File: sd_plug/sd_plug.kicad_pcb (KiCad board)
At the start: 2 copper layers, 44.2 x 20 mm, 4 parts, among them J1 MUX CONNECT TOP, J2 MUX CONNECT BOTTOM, P1 uSD PADS

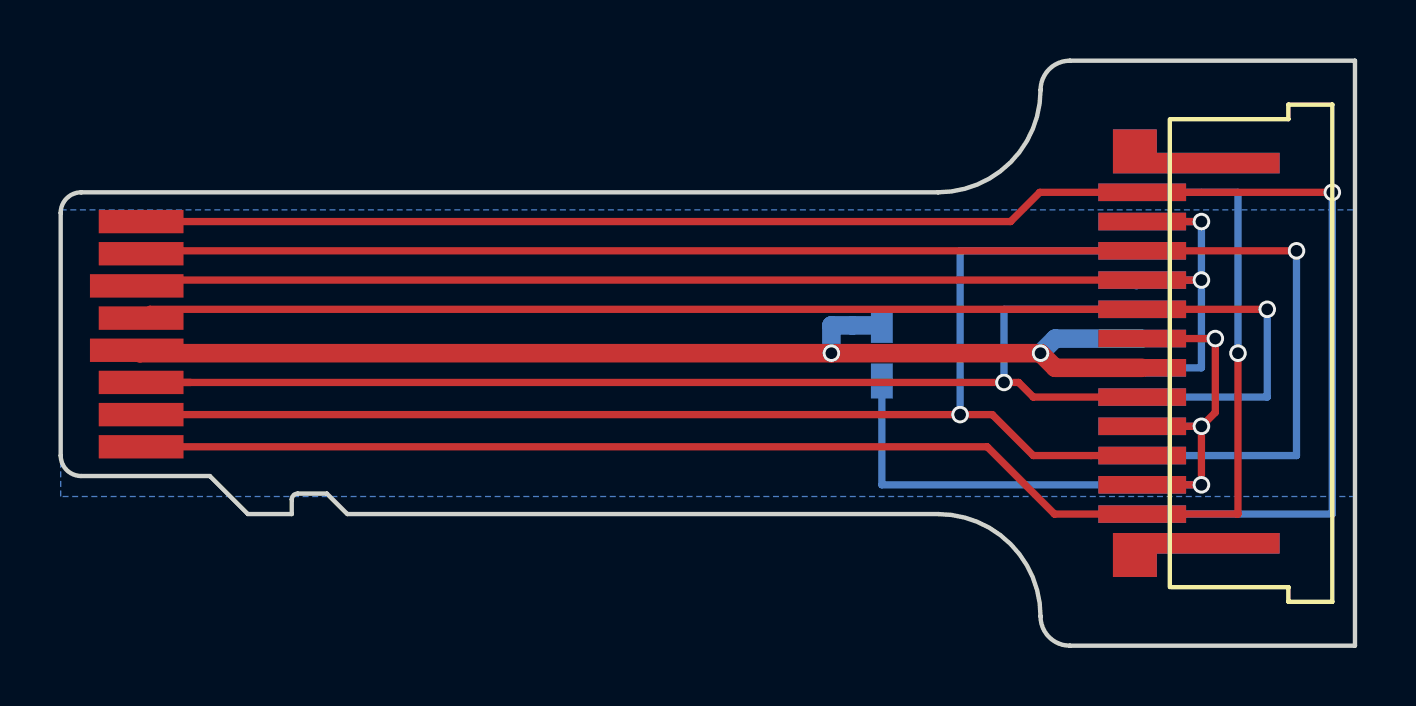
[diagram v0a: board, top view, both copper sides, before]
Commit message: renumbered FFC on adapter board
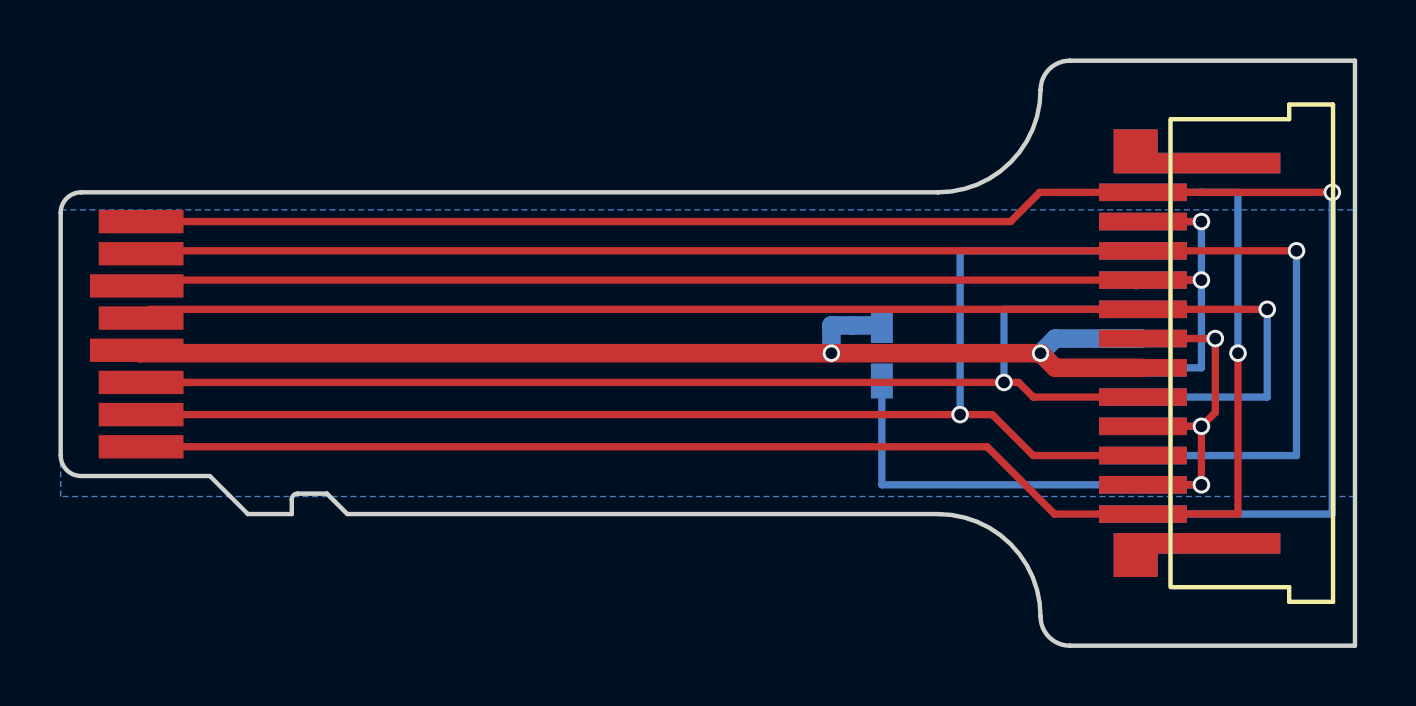
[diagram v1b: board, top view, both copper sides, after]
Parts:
- J1, J2: footprint sd_mux_footprints:FFC_connector_SFW12R-2STE1LF -> sd_plug_footprints:FFC_connector_SFW12R-2STE1LF_reversed
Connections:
- J1 pad 1: DAT2 -> DAT1
- J1 pad 10: DAT0 -> DAT3/CD
- J1 pad 12: DAT1 -> DAT2
- J1 pad 3: DAT3/CD -> DAT0
- J1 pad 5: CMD -> CLK
- J1 pad 6: VDD -> VSS
- J1 pad 7: VSS -> VDD
- J1 pad 8: CLK -> CMD
- J2 pad 1: DAT2 -> DAT1
- J2 pad 10: DAT0 -> DAT3/CD
- J2 pad 12: DAT1 -> DAT2
- J2 pad 3: DAT3/CD -> DAT0
- J2 pad 5: CMD -> CLK
- J2 pad 6: VDD -> VSS
- J2 pad 7: VSS -> VDD
- J2 pad 8: CLK -> CMD

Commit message: redid mounting holes on mux board
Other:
- rule pad_to_mask_clearance: 0.05 -> 0.127
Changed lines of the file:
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@@
   (general
     (links 26)
-    (no_connects 24)
+    (no_connects 0)
     (area 128.674999 97.574999 173.075001 117.725001)
     (thickness 1.6)
@@
     (pad_size 1.524 1.524)
     (pad_drill 0.762)
-    (pad_to_mask_clearance 0.05)
+    (pad_to_mask_clearance 0.127)
+    (solder_mask_min_width 0.0254)
     (aux_axis_origin 0 0)
     (grid_origin 128.75 102.15)
     (visible_elements FFFFFF7F)
     (pcbplotparams
-      (layerselection 0x00030_80000001)
+      (layerselection 0x010f0_80000001)
       (usegerberextensions false)
       (excludeedgelayer true)
@@
       (padsonsilk false)
       (subtractmaskfromsilk false)
-      (outputformat 1)
+      (outputformat 4)
       (mirror false)
-      (drillshape 1)
+      (drillshape 0)
       (scaleselection 1)
-      (outputdirectory ""))
+      (outputdirectory ../../pdfs/sd_plug/))
   )
   (net 0 "")

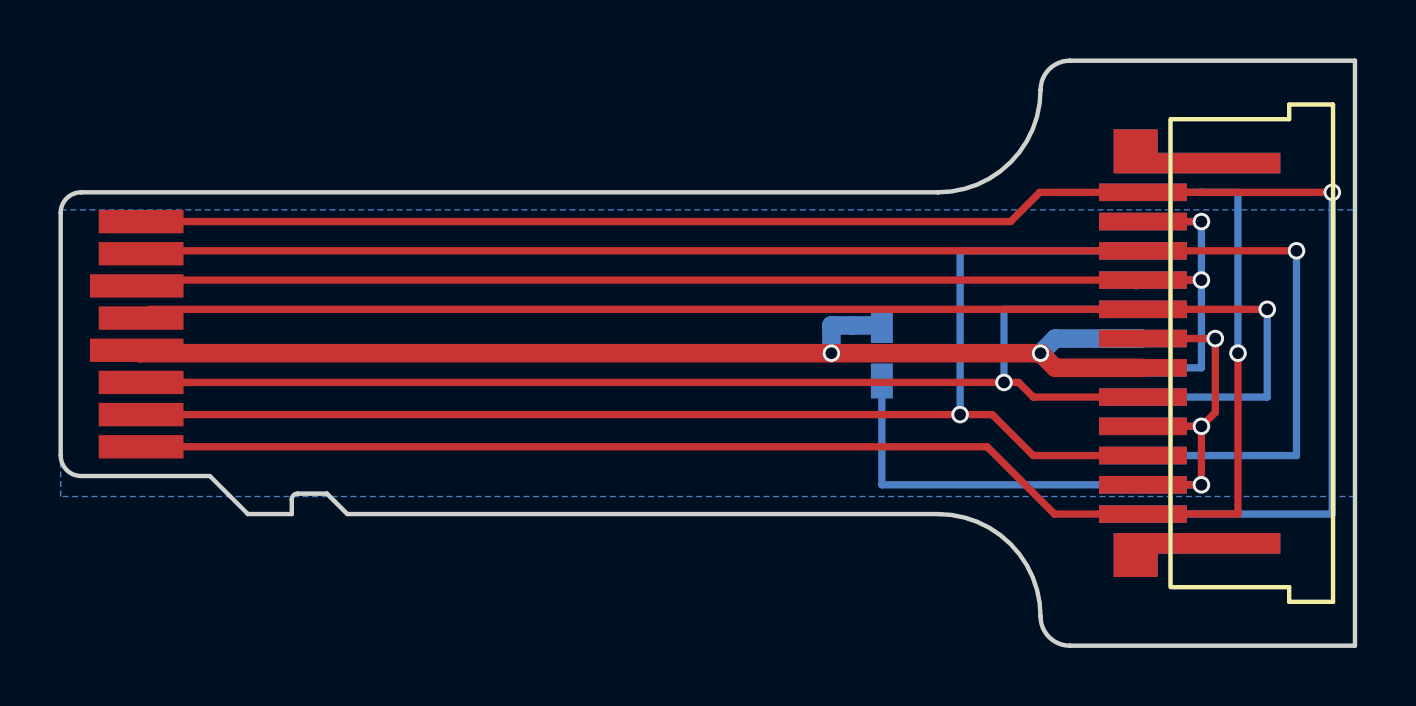
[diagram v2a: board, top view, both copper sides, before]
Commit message: rerouted mux board to fix FFC flip issue and fix tracks that had become unalaigned from the grid
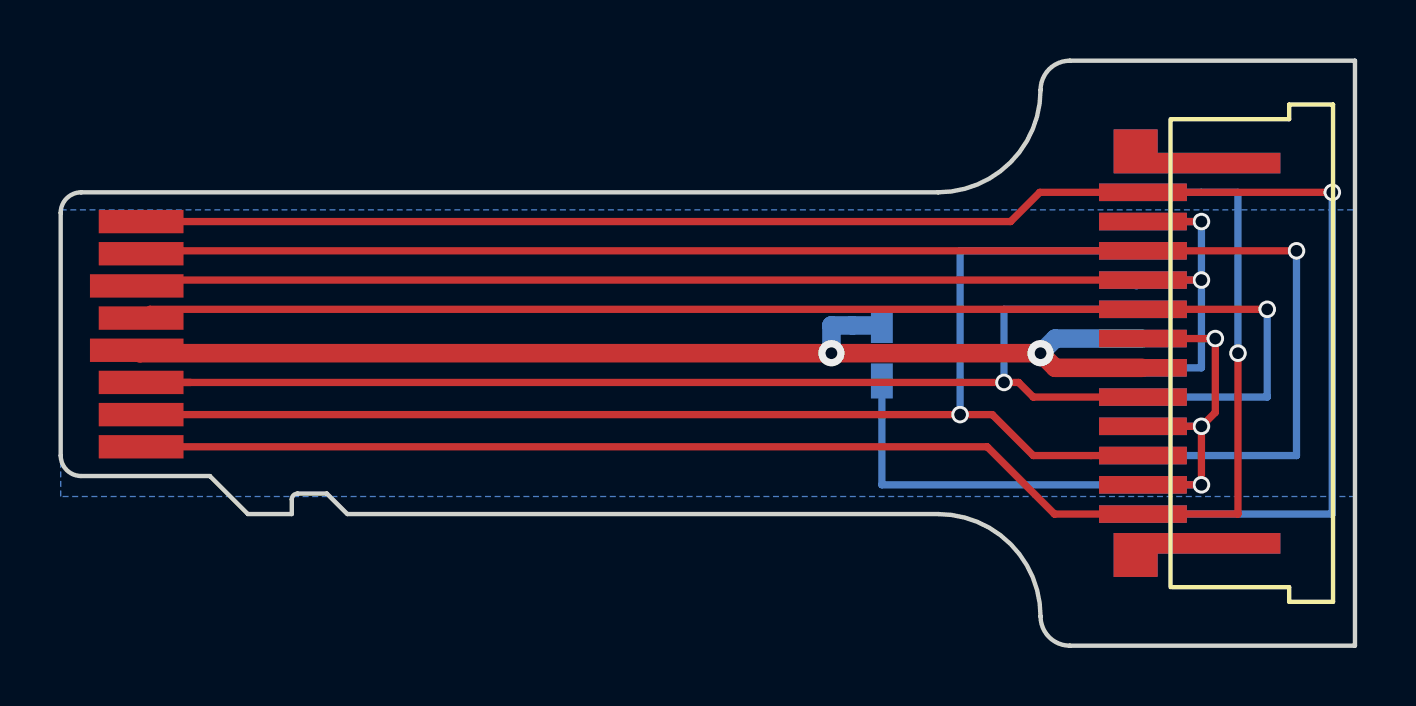
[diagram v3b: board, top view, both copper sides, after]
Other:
- rule pad_to_mask_clearance: 0.127 -> 0.15
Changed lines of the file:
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@@
     (links 26)
     (no_connects 0)
-    (area 128.674999 97.574999 173.075001 117.725001)
+    (area 112.350001 97.574999 173.075002 117.725001)
     (thickness 1.6)
     (drawings 26)
@@
     (pad_size 1.524 1.524)
     (pad_drill 0.762)
-    (pad_to_mask_clearance 0.127)
+    (pad_to_mask_clearance 0.15)
     (solder_mask_min_width 0.0254)
     (aux_axis_origin 0 0)
@@
   (segment (start 156.825 106.7) (end 155.815 106.7) (width 0.635) (layer B.Cu) (net 1))
   (segment (start 131.439972 107.639972) (end 131.35 107.55) (width 0.25) (layer F.Cu) (net 1))
-  (via (at 162.25 107.65) (size 0.6) (drill 0.4) (layers F.Cu B.Cu) (net 1))
+  (via (at 162.25 107.65) (size 0.9) (drill 0.4) (layers F.Cu B.Cu) (net 1))
   (segment (start 165.725 107.15) (end 162.75 107.15) (width 0.635) (layer B.Cu) (net 1))
   (segment (start 162.75 107.15) (end 162.25 107.65) (width 0.635) (layer B.Cu) (net 1))
@@
   (segment (start 162.25 107.65) (end 155.1 107.65) (width 0.635) (layer F.Cu) (net 1))
   (segment (start 162.75 108.15) (end 162.25 107.65) (width 0.635) (layer F.Cu) (net 1))
-  (via (at 155.1 107.65) (size 0.6) (drill 0.4) (layers F.Cu B.Cu) (net 1))
+  (via (at 155.1 107.65) (size 0.9) (drill 0.4) (layers F.Cu B.Cu) (net 1) (status 1000000))
   (segment (start 155.1 106.7) (end 155.1 107.65) (width 0.635) (layer B.Cu) (net 1))
   (segment (start 155.815 106.7) (end 155.1 106.7) (width 0.635) (layer B.Cu) (net 1))

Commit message: minor routing change to sd plug board
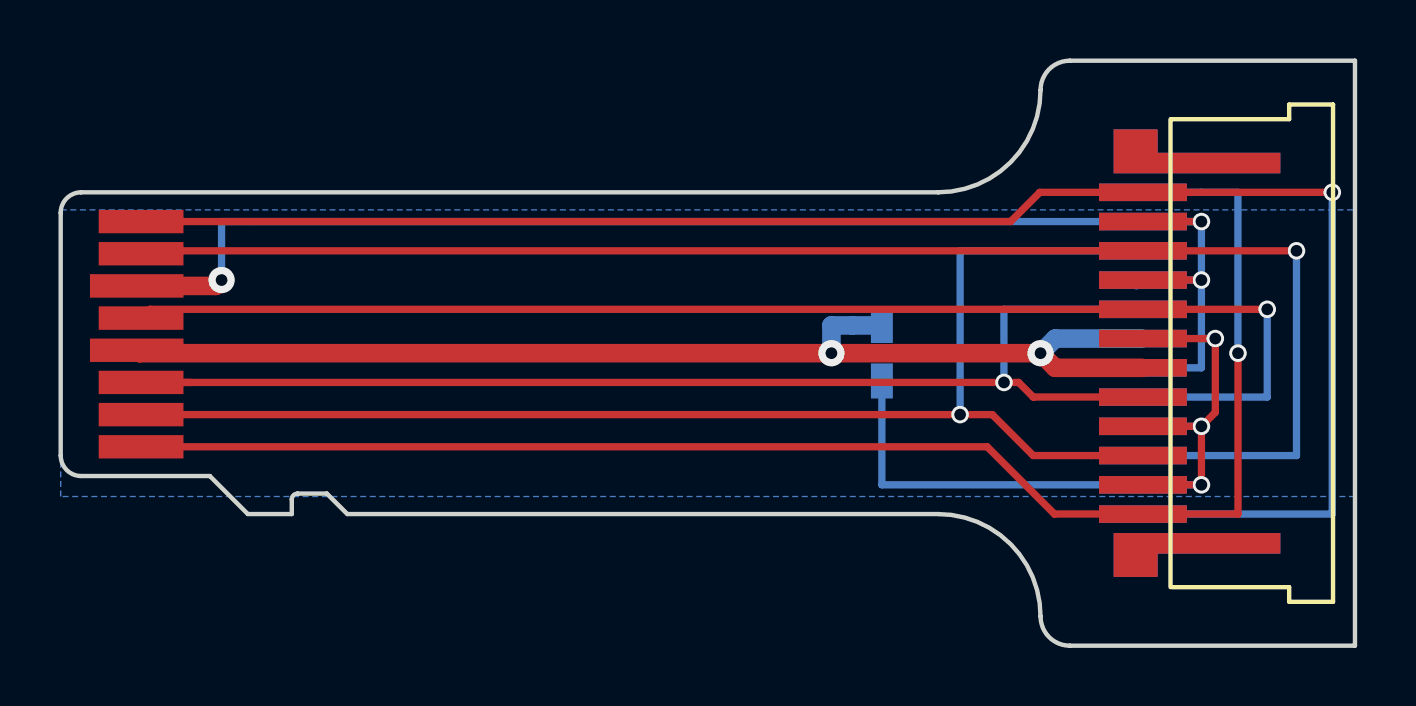
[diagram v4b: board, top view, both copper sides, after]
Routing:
- net VSS: track 78.8 -> 83.1 mm, vias 5 -> 6
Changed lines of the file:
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@@
     (links 26)
     (no_connects 0)
-    (area 112.350001 97.574999 173.075002 117.725001)
+    (area 128.674999 97.574999 173.075001 117.725001)
     (thickness 1.6)
     (drawings 26)
-    (tracks 85)
+    (tracks 90)
     (zones 0)
     (modules 4)
@@
   )
   (setup
-    (last_trace_width 0.25)
+    (last_trace_width 0.635)
     (user_trace_width 0.635)
     (trace_clearance 0.25)
@@
     (via_min_size 0.4)
     (via_min_drill 0.3)
+    (user_via 0.9 0.4)
     (uvia_size 0.3)
     (uvia_drill 0.1)
     (uvias_allowed no)
-    (uvia_min_size 0.2)
-    (uvia_min_drill 0.1)
+    (uvia_min_size 0)
+    (uvia_min_drill 0)
     (pcb_text_width 0.3)
     (pcb_text_size 1.5 1.5)
@@
   (segment (start 162.25 107.65) (end 155.1 107.65) (width 0.635) (layer F.Cu) (net 1))
   (segment (start 162.75 108.15) (end 162.25 107.65) (width 0.635) (layer F.Cu) (net 1))
-  (via (at 155.1 107.65) (size 0.9) (drill 0.4) (layers F.Cu B.Cu) (net 1) (status 1000000))
+  (via (at 155.1 107.65) (size 0.9) (drill 0.4) (layers F.Cu B.Cu) (net 1))
   (segment (start 155.1 106.7) (end 155.1 107.65) (width 0.635) (layer B.Cu) (net 1))
   (segment (start 155.815 106.7) (end 155.1 106.7) (width 0.635) (layer B.Cu) (net 1))
+  (segment (start 134.25 105.15) (end 134.05 105.35) (width 0.635) (layer F.Cu) (net 2))
+  (segment (start 134.05 105.35) (end 131.35 105.35) (width 0.635) (layer F.Cu) (net 2))
+  (segment (start 134.25 103.15) (end 134.25 105.15) (width 0.25) (layer B.Cu) (net 2))
+  (via (at 134.25 105.15) (size 0.9) (drill 0.4) (layers F.Cu B.Cu) (net 2))
+  (segment (start 135.25 103.15) (end 134.25 103.15) (width 0.25) (layer B.Cu) (net 2))
+  (segment (start 167.75 103.15) (end 135.25 103.15) (width 0.25) (layer B.Cu) (net 2))
   (segment (start 167.75 107.15) (end 168.225 107.15) (width 0.25) (layer B.Cu) (net 2))
   (via (at 168.225 107.15) (size 0.6) (drill 0.4) (layers F.Cu B.Cu) (net 2))
@@
   (segment (start 165.725 112.15) (end 156.825 112.15) (width 0.25) (layer B.Cu) (net 2))
   (segment (start 156.825 112.15) (end 156.825 108.6) (width 0.25) (layer B.Cu) (net 2))
-  (segment (start 165.725 105.15) (end 131.55 105.15) (width 0.25) (layer F.Cu) (net 2))
   (segment (start 131.55 105.15) (end 131.35 105.35) (width 0.25) (layer F.Cu) (net 2))
   (segment (start 167.75 112.15) (end 167.75 110.15) (width 0.25) (layer F.Cu) (net 2))
